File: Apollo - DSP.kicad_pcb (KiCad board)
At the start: 4 copper layers, 74.9 x 58 mm, 88 parts, among them J1 USB_C_Receptacle_USB2.0, J2 Conn_01x04, J3 Conn_01x04, J4 MEM2067-02-180-00-A_REVB, J5 Conn_01x06, U1 NCP115ASN330T2G, U2 NCP115ASN330T2G, U3 USBLC6-2SC6, U4 STM32F401RBTx, U5 23K256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

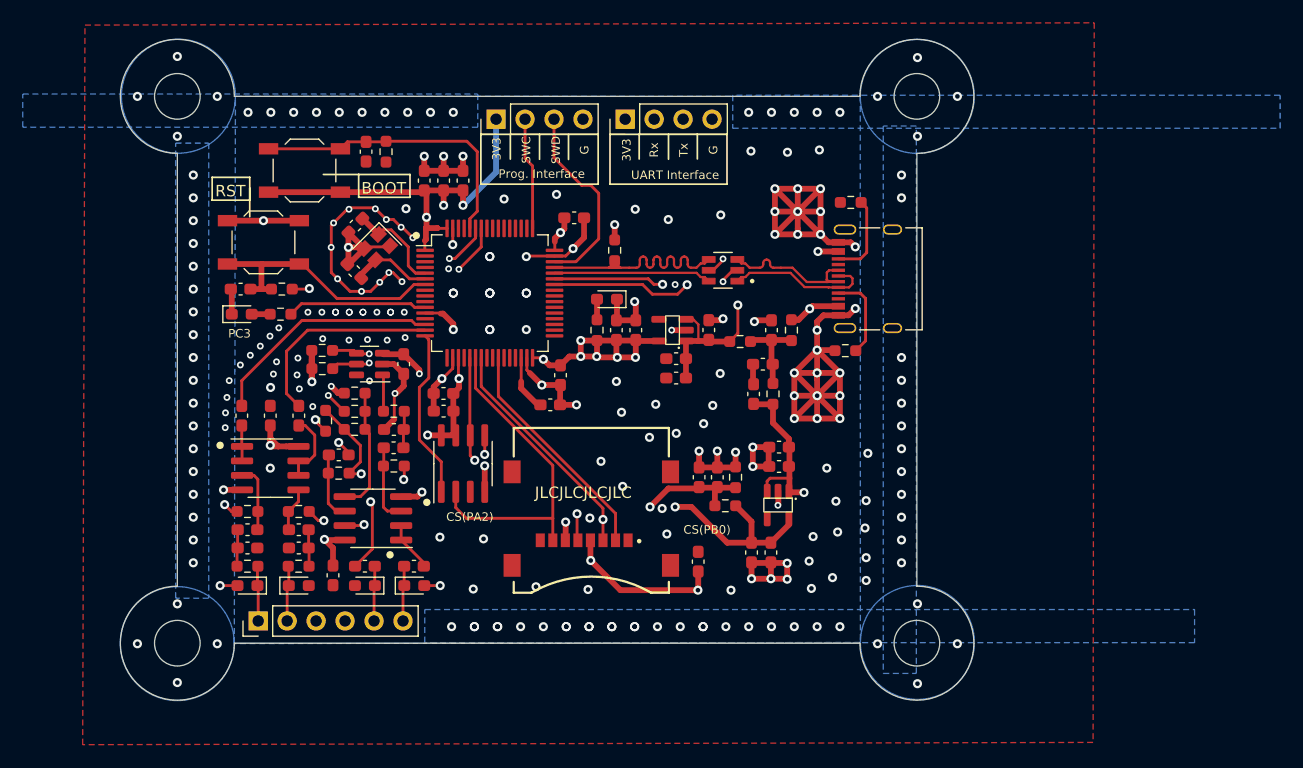
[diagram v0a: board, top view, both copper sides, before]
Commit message: fixed bootloader setting to SWD, removed boot button.
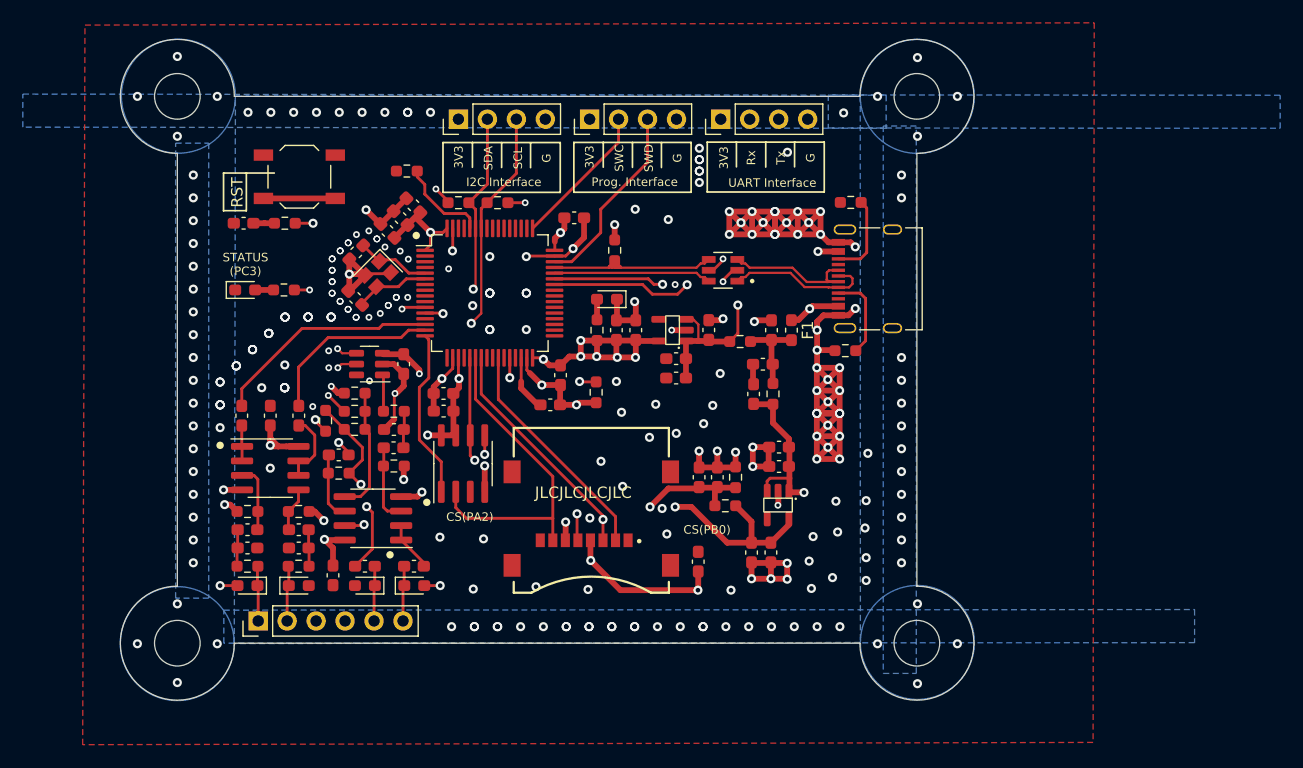
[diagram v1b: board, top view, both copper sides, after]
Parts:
- removed BOOT1: BOOT0, Button_Switch_SMD:SW_SPST_TL3342
- removed C22: 100n, Capacitor_SMD:C_0603_1608Metric_Pad1.08x0.95mm_HandSolder
- added J6: Conn_01x04, Connector_PinHeader_2.54mm:PinHeader_1x04_P2.54mm_Vertical, F.Cu at (124.5, 63.7)
- added R22: 10k, Resistor_SMD:R_0603_1608Metric_Pad0.98x0.95mm_HandSolder, F.Cu at (136.6, 87.7)
- F1: footprint Resistor_SMD:R_0603_1608Metric_Pad0.98x0.95mm_HandSolder -> Fuse:Fuse_0603_1608Metric_Pad1.05x0.95mm_HandSolder
- R1: value 300R -> 470R
- moved R9 21.2 mm to (127.9, 71.0), turned to 0 degrees
- moved R10 17.6 mm to (124.5, 71.0)
- moved J3 8.38 mm to (147.5, 63.7)
- moved J2 8.20 mm to (136.0, 63.7)
- moved RESET1 6.56 mm to (110.5, 68.8)
- moved R6 5.78 mm to (109.3, 72.8)
- moved C21 5.78 mm to (105.7, 72.8)
- moved C18 5.47 mm to (118.3, 73.5), turned to 135 degrees
- moved C20 5.01 mm to (119.4, 72.4), turned to 135 degrees
- moved C19 4.86 mm to (120.5, 71.2), turned to 135 degrees
- moved R7 2.49 mm to (120.0, 68.2), turned to 180 degrees
- moved Y1 2.35 mm to (117.4, 77.3)
- moved C24 2.35 mm to (115.5, 75.4)
- moved C25 2.35 mm to (115.4, 79.4)
- moved D2 2.15 mm to (105.8, 78.7)
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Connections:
- U4 pad 28: unconnected-(U4-PB2-Pad28) -> BOOT1
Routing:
- net 3.3V: track 95.1 -> 64.8 mm, vias 17 -> 16
- net BOOT0: track 25.9 -> 8.03 mm
- net NRST: track 23.1 -> 8.41 mm
- net SCL: track 22.1 -> 34.6 mm
- net SDA: track 20.8 -> 32.6 mm
- net GND: track 226.8 -> 216.1 mm, vias 246 -> 274
- net BOOT1: track 0.00 -> 9.68 mm, vias 0 -> 2
- net USB_D+: track 22.6 -> 18.6 mm
- net Tx: track 27.0 -> 30.2 mm
- net Rx: track 24.5 -> 27.3 mm
- net SWCLK: track 9.85 -> 12.7 mm
- net Net-(U4-PC3): track 12.3 -> 14.7 mm, vias 0 -> 2
- net ADC_CH1_IN: track 18.1 -> 15.8 mm
- net X1: track 8.80 -> 6.55 mm
- net USB_CONN_+: track 13.7 -> 12.8 mm
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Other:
- board text added: "APOLLO - DSP"
- board text added: "I2C Interface"
- board text added: "SCL"
- board text added: "SDA"
- board text added: "STATUS (PC3)"
- board text removed: "APOLLO-DSP"
- board text removed: "BOOT"
- board text removed: "PC3"

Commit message: some changes
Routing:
- net NRST: track 8.41 -> 32.5 mm, vias 0 -> 2
- net Net-(C40-Pad1): track 18.3 -> 16.3 mm
- net Net-(R16-Pad1): track 15.1 -> 14.0 mm
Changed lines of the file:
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@@
     (pad "S1" thru_hole oval (at 4.32 2.24 180) (size 1.7 0.9) (drill oval 1.4 0.6) (layers "*.Cu" "*.Mask")
       (net 22 "unconnected-(J1-SHIELD-PadS1)") (pinfunction "SHIELD") (pintype "passive+no_connect"))
-    (model "${KICAD6_3DMODEL_DIR}/Connector_USB.3dshapes/USB4105-GF-A--3DModel-STEP-56544.STEP"
-      (offset (xyz 0 -2.5 0))
+    (model "${KICAD7_3DMODEL_DIR}/Connector_USB.3dshapes/USB_C_Receptacle_GCT_USB4105-xx-A_16P_TopMnt_Horizontal.step"
+      (offset (xyz 0 -1.5 0))
       (scale (xyz 1 1 1))
-      (rotate (xyz -90 0 0))
+      (rotate (xyz 0 0 0))
     )
   )
@@
   (segment (start 118.975 76.025) (end 117.7 76.025) (width 0.254) (layer "F.Cu") (net 9))
   (segment (start 117.543983 76.16334) (end 116.147796 74.767153) (width 0.254) (layer "F.Cu") (net 9))
+  (segment (start 107.4 72.7375) (end 107.4875 72.825) (width 0.508) (layer "F.Cu") (net 10))
   (segment (start 108.3625 72.825) (end 107.4875 72.825) (width 0.508) (layer "F.Cu") (net 10))
+  (segment (start 107.45 72.8625) (end 107.4875 72.825) (width 0.2) (layer "F.Cu") (net 10))
+  (segment (start 107.4 70.65) (end 107.4 72.7375) (width 0.508) (layer "F.Cu") (net 10))
+  (segment (start 121.575 78.2) (end 123.2 78.2) (width 0.2) (layer "F.Cu") (net 10))
   (segment (start 107.4 70.65) (end 113.7 70.65) (width 0.508) (layer "F.Cu") (net 10))
+  (segment (start 107.45 74.2) (end 107.45 72.8625) (width 0.2) (layer "F.Cu") (net 10))
   (segment (start 113.7 70.65) (end 113.975 70.65) (width 0.254) (layer "F.Cu") (net 10))
   (segment (start 107.4875 72.825) (end 106.525001 72.825) (width 0.508) (layer "F.Cu") (net 10))
+  (via (at 123.2 78.2) (size 0.6) (drill 0.3) (layers "F.Cu" "B.Cu") (net 10))
+  (via (at 107.45 74.2) (size 0.6) (drill 0.3) (layers "F.Cu" "B.Cu") (net 10))
+  (segment (start 123.2 77.85) (end 118 72.65) (width 0.2) (layer "In2.Cu") (net 10))
+  (segment (start 114.7 72.65) (end 113.15 74.2) (width 0.2) (layer "In2.Cu") (net 10))
+  (segment (start 113.15 74.2) (end 107.45 74.2) (width 0.2) (layer "In2.Cu") (net 10))
+  (segment (start 118 72.65) (end 114.7 72.65) (width 0.2) (layer "In2.Cu") (net 10))
+  (segment (start 123.2 78.2) (end 123.2 77.85) (width 0.2) (layer "In2.Cu") (net 10))
   (segment (start 130 84.625) (end 130 86.7) (width 0.254) (layer "F.Cu") (net 11))
   (segment (start 130 87.3) (end 130 86.7) (width 0.508) (layer "F.Cu") (net 11))
@@
   (segment (start 121.4625 102.5925) (end 121.4625 102.9) (width 0.254) (layer "F.Cu") (net 88))
   (segment (start 111.95 90.05) (end 111.95 90.1625) (width 0.25) (layer "F.Cu") (net 89))
-  (segment (start 116.45 97.675) (end 116.95 98.175) (width 0.25) (layer "F.Cu") (net 89))
-  (segment (start 116.95 98.175) (end 116.95 101.3875) (width 0.25) (layer "F.Cu") (net 89))
-  (segment (start 116.95 101.3875) (end 115.4375 102.9) (width 0.25) (layer "F.Cu") (net 89))
+  (segment (start 116.145421 100.045482) (end 116.15 100.050061) (width 0.25) (layer "F.Cu") (net 89))
   (segment (start 111.95 90.1625) (end 112.85 91.0625) (width 0.25) (layer "F.Cu") (net 89))
+  (segment (start 116.15 102.1875) (end 115.4375 102.9) (width 0.25) (layer "F.Cu") (net 89))
+  (segment (start 116.15 100.050061) (end 116.15 102.1875) (width 0.25) (layer "F.Cu") (net 89))
   (via (at 111.95 90.05) (size 0.8) (drill 0.4) (layers "F.Cu" "B.Cu") (net 89))
-  (via (at 116.45 97.675) (size 0.8) (drill 0.4) (layers "F.Cu" "B.Cu") (net 89))
-  (segment (start 113.7 97.25) (end 111.95 95.5) (width 0.25) (layer "In2.Cu") (net 89))
-  (segment (start 116.025 97.25) (end 113.7 97.25) (width 0.25) (layer "In2.Cu") (net 89))
-  (segment (start 111.95 95.5) (end 111.95 90.05) (width 0.25) (layer "In2.Cu") (net 89))
-  (segment (start 116.45 97.675) (end 116.025 97.25) (width 0.25) (layer "In2.Cu") (net 89))
+  (via (at 116.145421 100.045482) (size 0.6) (drill 0.3) (layers "F.Cu" "B.Cu") (net 89))
+  (segment (start 115.966616 99.875) (end 111.95 95.858384) (width 0.25) (layer "In2.Cu") (net 89))
+  (segment (start 115.974939 99.875) (end 115.966616 99.875) (width 0.25) (layer "In2.Cu") (net 89))
+  (segment (start 116.145421 100.045482) (end 115.974939 99.875) (width 0.25) (layer "In2.Cu") (net 89))
+  (segment (start 111.95 95.858384) (end 111.95 90.05) (width 0.25) (layer "In2.Cu") (net 89))
   (segment (start 113.0875 97.3875) (end 113.765 98.065) (width 0.254) (layer "F.Cu") (net 90))
   (segment (start 113.765 98.065) (end 114.525 98.065) (width 0.254) (layer "F.Cu") (net 90))
@@
   (segment (start 116.3125 90.9) (end 116.3125 89.32) (width 0.254) (layer "F.Cu") (net 91))
   (segment (start 116.3125 89.32) (end 116.3125 87.725) (width 0.254) (layer "F.Cu") (net 91))
-  (segment (start 116.7 91.2875) (end 116.7 96) (width 0.254) (layer "F.Cu") (net 91))
-  (segment (start 116.7 96) (end 115.905 96.795) (width 0.254) (layer "F.Cu") (net 91))
-  (segment (start 115.905 96.795) (end 114.525 96.795) (width 0.254) (layer "F.Cu") (net 91))
+  (segment (start 116.7 91.2875) (end 116.7 95.9) (width 0.254) (layer "F.Cu") (net 91))
+  (segment (start 115.805 96.795) (end 114.525 96.795) (width 0.254) (layer "F.Cu") (net 91))
+  (segment (start 116.7 95.9) (end 115.805 96.795) (width 0.254) (layer "F.Cu") (net 91))
   (segment (start 116.3125 90.9) (end 116.7 91.2875) (width 0.254) (layer "F.Cu") (net 91))
   (segment (start 121.575 80.2) (end 119.7 80.2) (width 0.254) (layer "F.Cu") (net 92))
@@
   (segment (start 112.325 79.55) (end 111.45 78.675) (width 0.254) (layer "In2.Cu") (net 92))
   (segment (start 114.4875 90.875) (end 112.85 89.2375) (width 0.25) (layer "F.Cu") (net 93))
+  (segment (start 114.85 95.8) (end 114.9125 95.7375) (width 0.25) (layer "F.Cu") (net 93))
+  (segment (start 114.9125 95.7375) (end 114.9125 94.74) (width 0.25) (layer "F.Cu") (net 93))
   (segment (start 114.4875 90.9) (end 114.5 90.9) (width 0.25) (layer "F.Cu") (net 93))
   (segment (start 114.5 90.9) (end 116.075 92.475) (width 0.25) (layer "F.Cu") (net 93))
-  (segment (start 116.1405 99.335) (end 116.2255 99.25) (width 0.25) (layer "F.Cu") (net 93))
-  (segment (start 115.948036 95.724536) (end 115.897036 95.724536) (width 0.25) (layer "F.Cu") (net 93))
+  (segment (start 116.45 98.5) (end 115.615 99.335) (width 0.25) (layer "F.Cu") (net 93))
   (segment (start 116.075 93.5775) (end 114.9125 94.74) (width 0.25) (layer "F.Cu") (net 93))
+  (segment (start 116.45 98.2) (end 116.45 98.5) (width 0.25) (layer "F.Cu") (net 93))
   (segment (start 114.4875 90.9) (end 114.4875 90.875) (width 0.25) (layer "F.Cu") (net 93))
-  (segment (start 115.897036 95.724536) (end 114.9125 94.74) (width 0.25) (layer "F.Cu") (net 93))
-  (segment (start 114.525 99.335) (end 116.1405 99.335) (width 0.25) (layer "F.Cu") (net 93))
+  (segment (start 115.615 99.335) (end 114.525 99.335) (width 0.25) (layer "F.Cu") (net 93))
   (segment (start 116.075 92.475) (end 116.075 93.5775) (width 0.25) (layer "F.Cu") (net 93))
-  (via (at 115.948036 95.724536) (size 0.8) (drill 0.4) (layers "F.Cu" "B.Cu") (net 93))
-  (via (at 116.2255 99.25) (size 0.8) (drill 0.4) (layers "F.Cu" "B.Cu") (net 93))
-  (segment (start 117.35 98.1255) (end 116.2255 99.25) (width 0.25) (layer "In2.Cu") (net 93))
-  (segment (start 117.35 97.1265) (end 117.35 98.1255) (width 0.25) (layer "In2.Cu") (net 93))
-  (segment (start 115.948036 95.724536) (end 117.35 97.1265) (width 0.25) (layer "In2.Cu") (net 93))
+  (via (at 114.85 95.8) (size 0.6) (drill 0.3) (layers "F.Cu" "B.Cu") (net 93))
+  (via (at 116.45 98.2) (size 0.6) (drill 0.3) (layers "F.Cu" "B.Cu") (net 93))
+  (segment (start 114.85 95.85) (end 114.85 95.8) (width 0.25) (layer "In2.Cu") (net 93))
+  (segment (start 116.45 97.45) (end 114.85 95.85) (width 0.25) (layer "In2.Cu") (net 93))
+  (segment (start 116.45 98.2) (end 116.45 97.45) (width 0.25) (layer "In2.Cu") (net 93))
   (zone (net 2) (net_name "GND") (layer "F.Cu") (hatch edge 0.508)
     (connect_pads (clearance 0.508))

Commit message: modifications for rev 3
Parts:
- removed C10, C12, C28: 100n, Capacitor_SMD:C_0603_1608Metric_Pad1.08x0.95mm_HandSolder
- removed C11, C7, C8, C9: 10u, Capacitor_SMD:C_0603_1608Metric_Pad1.08x0.95mm_HandSolder
- removed FB2: 100R@100MHz, Resistor_SMD:R_0603_1608Metric_Pad0.98x0.95mm_HandSolder
- removed U2: NCP115ASN330T2G, NCP115ASN330T2G:NCP115ASN330T2G
- added R23: 10k, Resistor_SMD:R_0603_1608Metric_Pad0.98x0.95mm_HandSolder, F.Cu at (138.2, 87.7)
- R8: value 300 -> 1k
- moved R5 23.1 mm to (126.8, 102.3)
- moved R4 23.1 mm to (126.0, 104.8)
- moved C13 23.1 mm to (125.2, 102.3)
- moved C14 23.1 mm to (123.7, 102.3)
- moved C4 2.82 mm to (146.2, 85.3), turned to -90 degrees
- moved C2 2.81 mm to (149.2, 81.6), turned to 0 degrees
- moved C3 1.12 mm to (144.5, 85.3), turned to -90 degrees
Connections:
- C29 pad 2: +3.3VA -> 3.3V
- C39 pad 2: +5VA -> +5V
- C42 pad 2: +5VA -> +5V
- R21 pad 1: +5VA -> +5V
- R4 pad 2: +3.3VA -> 3.3V
- U6 pad 3: +3.3VA -> 3.3V
- U7 pad 8: +5VA -> +5V
- U8 pad 8: +5VA -> +5V
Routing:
- net +5VA: track 101.5 -> 0.00 mm, vias 4 -> 0
- net +5V: track 20.1 -> 83.4 mm, vias 2 -> 7
- net +3.3VA: track 47.7 -> 0.00 mm, vias 2 -> 0
- net VAA: track 61.2 -> 42.0 mm, vias 4 -> 3
- net 3.3V: track 64.8 -> 56.6 mm, vias 16 -> 17
- net VBUS: track 7.59 -> 3.40 mm
- net BOOT1: track 9.68 -> 11.3 mm
- net MOSI: track 34.8 -> 34.0 mm
- net Net-(U8B--): track 5.99 -> 5.16 mm
- net USB_D+: track 18.6 -> 17.8 mm
- net GND: track 216.1 -> 215.5 mm, vias 274 -> 205
- net Net-(J1-CC2): track 7.59 -> 7.05 mm

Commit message: ready for order
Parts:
- removed D3, D4, D5, D6: CG060312G, Diode_SMD:D_0603_1608Metric_Pad1.05x0.95mm_HandSolder
- added C7: 220u, Capacitor_SMD:C_0603_1608Metric_Pad1.08x0.95mm_HandSolder, F.Cu at (152.4, 85.1)
- added C8: 10u, Capacitor_SMD:C_0603_1608Metric_Pad1.08x0.95mm_HandSolder, F.Cu at (152.4, 86.6)
- added L1: 8u8, Inductor_SMD:L_0603_1608Metric_Pad1.05x0.95mm_HandSolder, F.Cu at (149.9, 85.9)
- added R24: 10R, Resistor_SMD:R_0603_1608Metric_Pad0.98x0.95mm_HandSolder, F.Cu at (148.3, 85.9)
- R1: value 470R -> 1k
- U3: footprint SnapEDA Library:SOT95P280X145-6N -> Package_TO_SOT_SMD:SOT-23-6_Handsoldering
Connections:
- C39 pad 2: +5V -> +5VA
- C42 pad 2: +5V -> +5VA
- R21 pad 1: +5V -> +5VA
- U7 pad 8: +5V -> +5VA
- U8 pad 8: +5V -> +5VA
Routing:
- net +5VA: track 0.00 -> 79.4 mm, vias 0 -> 5
- net +5V: track 83.4 -> 20.0 mm, vias 7 -> 2
- net GND: track 215.5 -> 202.7 mm, vias 205 -> 189
- net 3.3V: track 56.6 -> 66.8 mm
- net Net-(L1-Pad1): track 0.00 -> 1.54 mm

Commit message: checking for possible mistakes
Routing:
- net +5VA: track 79.4 -> 80.2 mm
- net GND: vias 189 -> 220

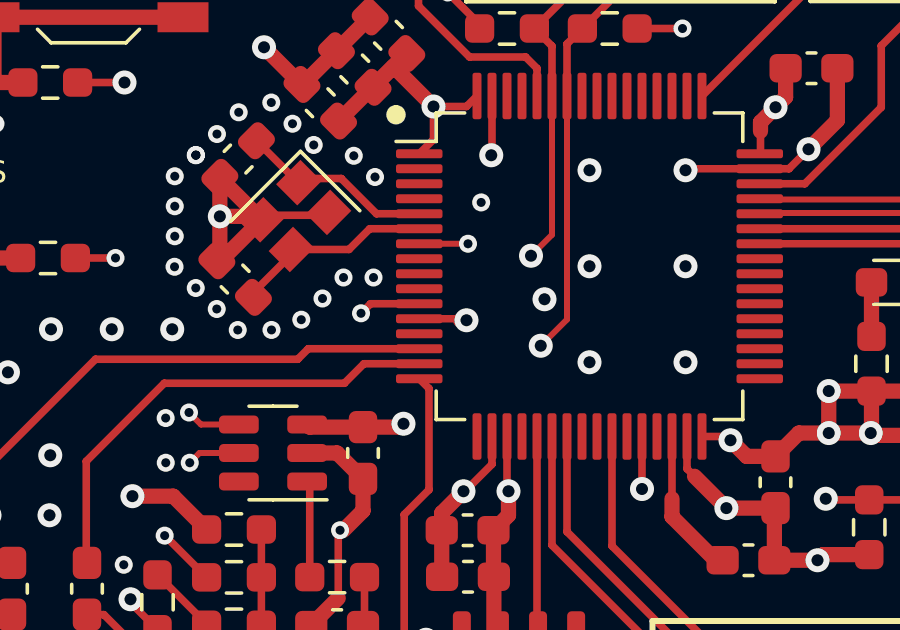
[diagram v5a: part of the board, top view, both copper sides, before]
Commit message: FIXED ADCVOLTAGE PIN
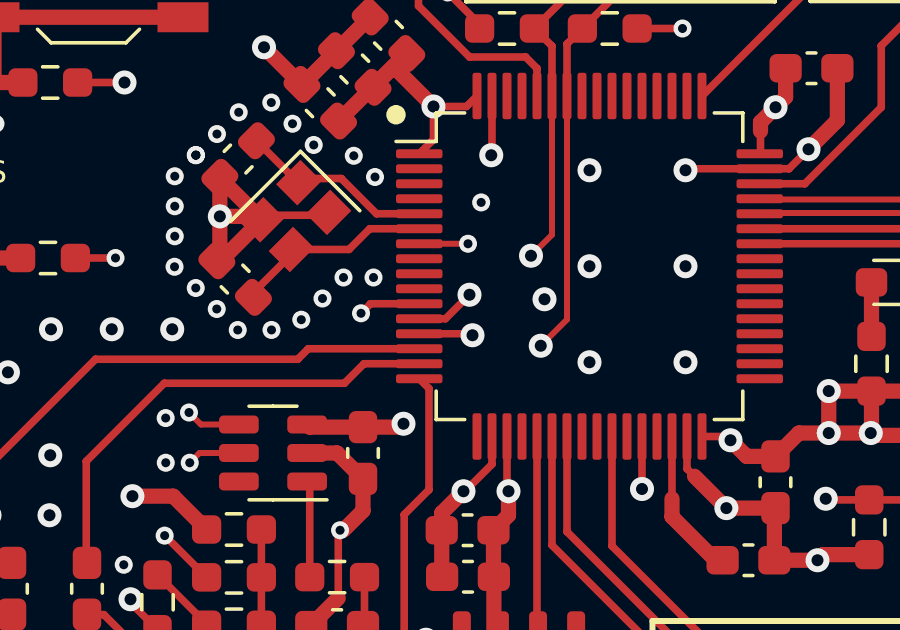
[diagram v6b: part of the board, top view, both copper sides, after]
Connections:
- U4 pad 13: unconnected-(U4-VREF+-Pad13) -> 3.3V
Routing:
- net 3.3V: track 66.8 -> 68.6 mm, vias 17 -> 18

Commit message: refreshing design
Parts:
- added TP1: TestPoint, TestPoint:TestPoint_Pad_D1.0mm, F.Cu at (120.9, 66.4)
- added TP2: TestPoint, TestPoint:TestPoint_Pad_D1.0mm, F.Cu at (134.9, 79.7)
- added TP3: TestPoint, TestPoint:TestPoint_Pad_D1.0mm, F.Cu at (134.9, 81.7)
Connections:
- U4 pad 36: unconnected-(U4-PB15-Pad36) -> Net-(U4-PB15)
- U4 pad 39: unconnected-(U4-PC8-Pad39) -> Net-(U4-PC8)
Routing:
- net Net-(U4-PC3): track 14.7 -> 0.00 mm, vias 2 -> 0
- net Net-(U4-PB15): track 0.00 -> 2.20 mm
- net BOOT0: track 8.03 -> 10.1 mm
- net Net-(U4-PC8): track 0.00 -> 2.02 mm
- net GND: vias 220 -> 188

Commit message: cleanup
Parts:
- moved TP3 10.5 mm to (142.2, 89.2)
- moved TP2 9.68 mm to (142.2, 86.0)
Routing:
- net Net-(U4-PC3): track 0.00 -> 12.7 mm
- net Net-(U4-PB15): track 2.20 -> 13.8 mm, vias 0 -> 2
- net Net-(U4-PC8): track 2.02 -> 13.3 mm, vias 0 -> 2
- net GND: track 203.1 -> 199.4 mm, vias 188 -> 207
- net +5VA: track 80.2 -> 78.2 mm
